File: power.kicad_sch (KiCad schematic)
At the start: 0 parts

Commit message: power sheet
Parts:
- added C1, C10, C15, C16, C21, C22, C4, C9: 1u, symbol Device:C_Small
- added C11, C13, C17, C19, C2, C23, C5, C7: 10u, symbol Device:C_Small
- added C12, C14, C18, C20, C24, C3, C6, C8: 100n, symbol Device:C_Small
- added L1, L2, L3, L4: 4u7, symbol Device:L_Small
- added R1, R7: 40k2, symbol Device:R_Small
- added R10: 249k, symbol Device:R_Small
- added R11: 20k5, symbol Device:R_Small
- added R12: 41k2, symbol Device:R_Small
- added R13, R4, R5, R9: 1k, symbol Device:R_Small
- added R14, R3: 75k, symbol Device:R_Small
- added R15: 11.375k, symbol Device:R_Small
- added R16, R2: 13k, symbol Device:R_Small
- added R6: 120k, symbol Device:R_Small
- added R8: 32k4, symbol Device:R_Small
- added TP1, TP4: 3V3, symbol Connector:TestPoint
- added TP2: 1V8, symbol Connector:TestPoint
- added TP3: 1V2, symbol Connector:TestPoint
- added U1, U2, U3, U4: MP1470, Package_TO_SOT_SMD:TSOT-23-6, symbol Regulator_Switching:MP1470
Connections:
- new net: C22.2, L4.1, U4.2 (SW)
- new net: R14.1, U4.4 (FB)
- new net: C21.1, R13.2, U4.5 (EN)
- new net: C22.1, U4.6 (BST)
- new net: R6.2, R7.2, R8.1
- new net: C1.2, L1.1, U1.2 (SW)
- new net: R6.1, U2.4 (FB)
- new net: R14.2, R15.2, R16.1
- new net: R3.1, U1.4 (FB)
- new net: C4.1, R4.2, U1.5 (EN)
- new net: C1.1, U1.6 (BST)
- new net: C9.1, R5.2, U2.5 (EN)
- new net: C16.2, L3.1, U3.2 (SW)
- new net: C15.1, R9.2, U3.5 (EN)
- new net: R10.2, R11.2, R12.1
- new net: C10.2, L2.1, U2.2 (SW)
- new net: C10.1, U2.6 (BST)
- new net: R1.2, R2.1, R3.2
- new net: R10.1, U3.4 (FB)
- new net: C16.1, U3.6 (BST)
- new net +1V2: C17.1, C18.1, L3.2, R11.1, TP3.1
- new net +1V5: C23.1, C24.1, L4.2, R15.1, TP4.1
- new net +1V8: C11.1, C12.1, L2.2, R7.1, TP2.1
- new net +3V3: C2.1, C3.1, L1.2, R1.1, TP1.1
- new net GND: C11.2, C12.2, C13.2, C14.2, C15.2, C17.2, C18.2, C19.2, C2.2, C20.2, C21.2, C23.2, C24.2, C3.2, C4.2, C5.2, C6.2, C7.2, C8.2, C9.2, R12.2, R16.2, R2.2, R8.2, U1.1 (GND), U2.1 (GND), U3.1 (GND), U4.1 (GND)
- new net VCC: C13.1, C14.1, C19.1, C20.1, C5.1, C6.1, C7.1, C8.1, R13.1, R4.1, R5.1, R9.1, U1.3 (IN), U2.3 (IN), U3.3 (IN), U4.3 (IN)
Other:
- note added: "+1V2 Rail"
- note added: "+1V5 Rail"
- note added: "+1V8 Rail"
- note added: "+3V3 Rail"

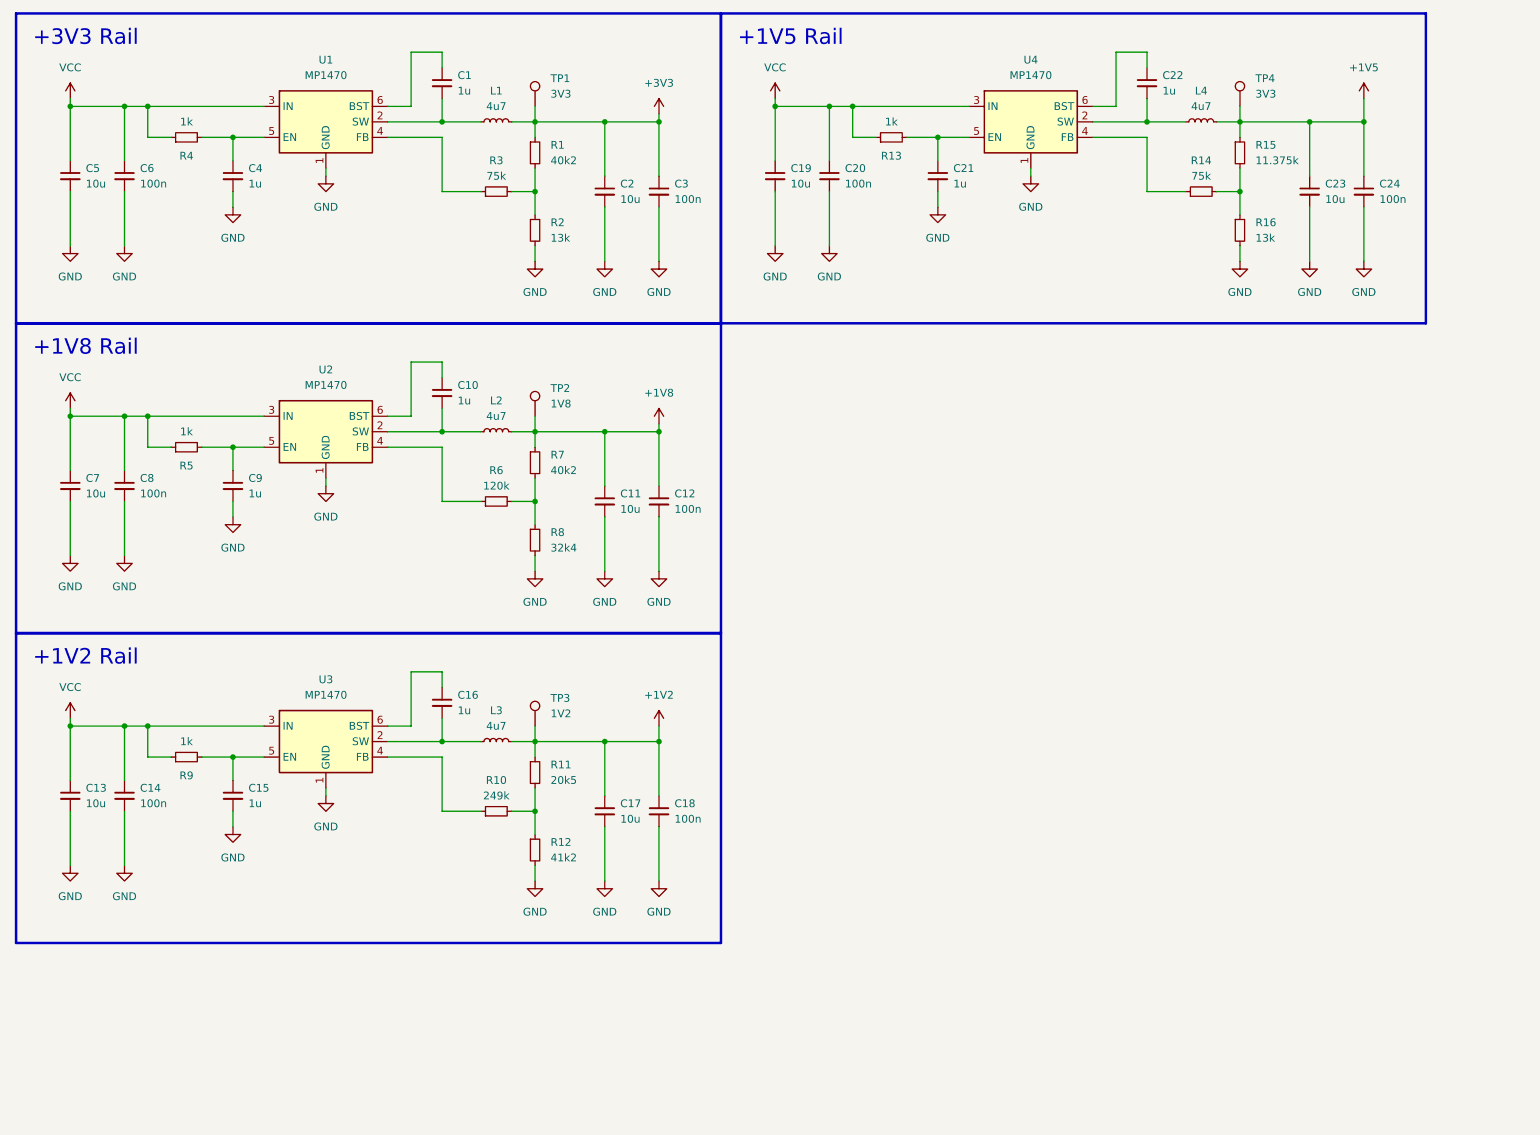
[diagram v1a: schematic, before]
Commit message: more power schematics, adding esd protection and reverse polarity protection and also a fuse.
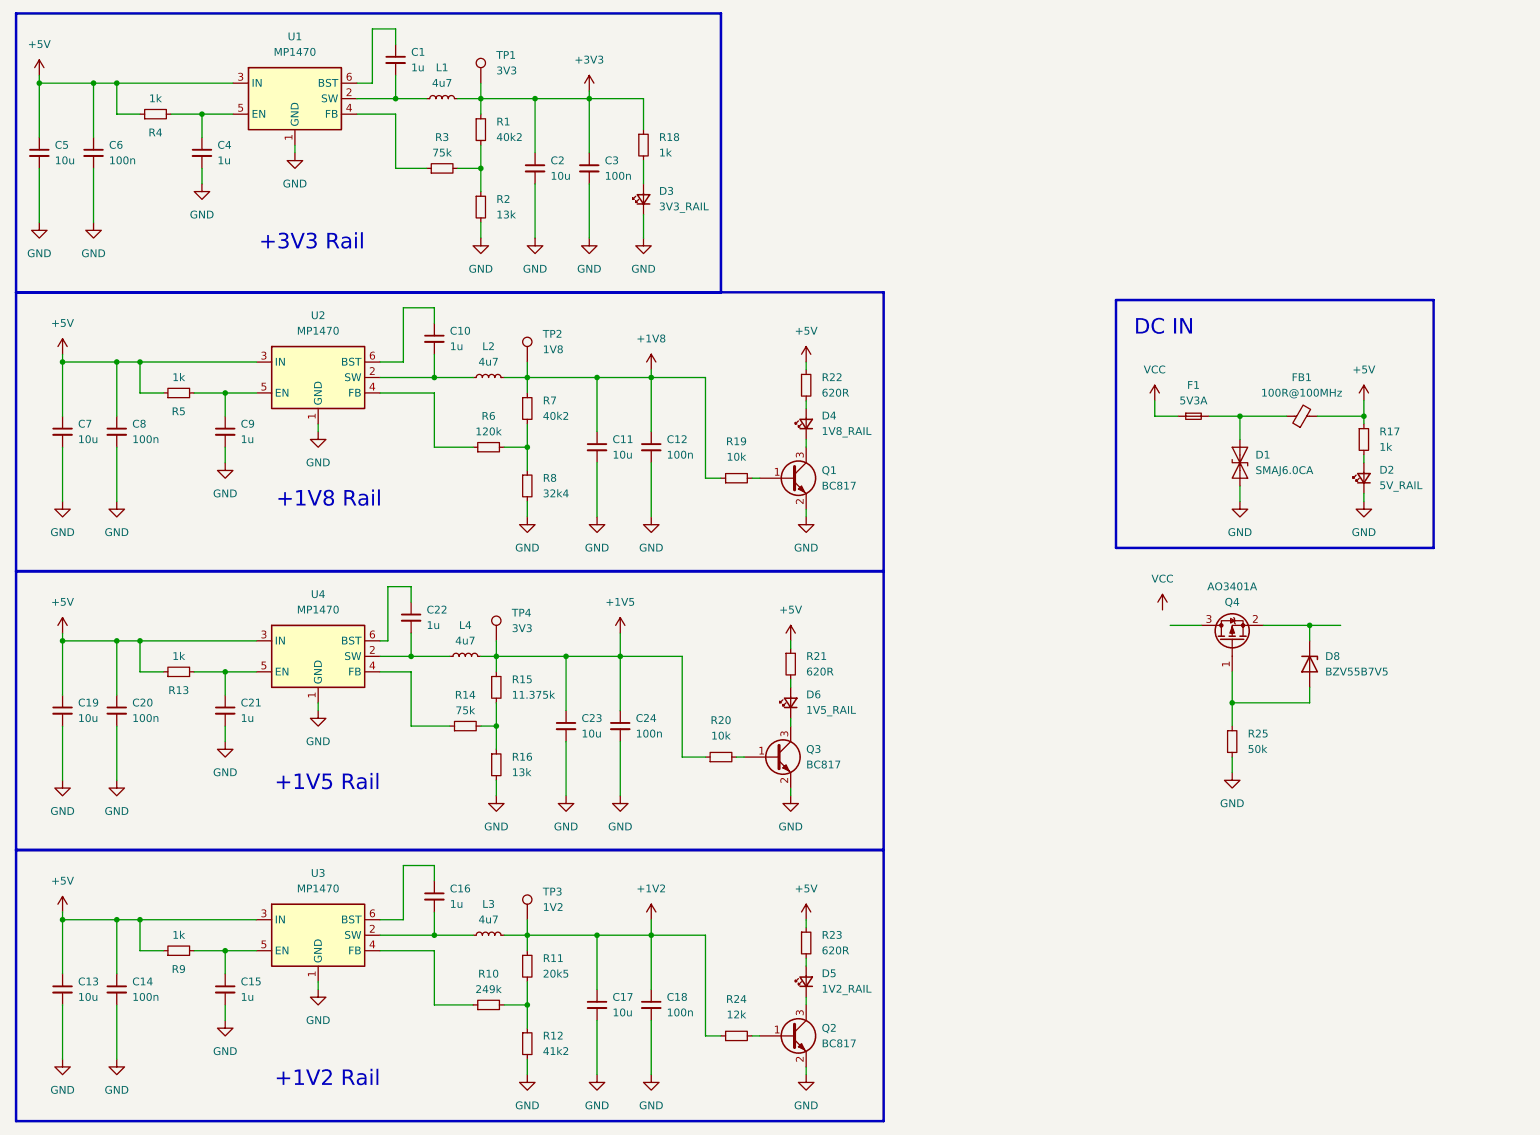
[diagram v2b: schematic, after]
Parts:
- added D1: SMAJ6.0CA, Diode_SMD:D_SMA, symbol Diode:SMAJ6.0CA
- added D2: 5V_RAIL, symbol Device:LED_Small
- added D3: 3V3_RAIL, symbol Device:LED_Small
- added D4: 1V8_RAIL, symbol Device:LED_Small
- added D5: 1V2_RAIL, symbol Device:LED_Small
- added D6: 1V5_RAIL, symbol Device:LED_Small
- added D8: BZV55B7V5, Diode_SMD:D_MiniMELF, symbol Diode:BZV55B7V5
- added F1: 5V3A, symbol Device:Fuse_Small
- added FB1: 100R@100MHz, symbol Device:FerriteBead_Small
- added Q1, Q2, Q3: BC817, Package_TO_SOT_SMD:SOT-23, symbol Transistor_BJT:BC817
- added Q4: AO3401A, Package_TO_SOT_SMD:SOT-23, symbol Transistor_FET:AO3401A
- added R17, R18: 1k, symbol Device:R_Small
- added R19, R20: 10k, symbol Device:R_Small
- added R21, R22, R23: 620R, symbol Device:R_Small
- added R24: 12k, symbol Device:R_Small
- added R25: 50k, symbol Device:R_Small
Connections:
- net +1V2: now also R24.1
- net +1V5: now also R20.1
- net +1V8: now also R19.1
- net +3V3: now also R18.1
- net GND: now also D1.1 (A1), D2.1 (K), D3.1 (K), Q1.2 (E), Q2.2 (E), Q3.2 (E), R25.2
- net VCC: now also F1.1; no longer C13.1, C14.1, C19.1, C20.1, C5.1, C6.1, C7.1, C8.1, R13.1, R4.1, R5.1, R9.1, U1.3 (IN), U2.3 (IN), U3.3 (IN), U4.3 (IN)
- new net: D6.1 (K), Q3.3 (C)
- new net: D6.2 (A), R21.2
- new net: Q1.1 (B), R19.2
- new net: D4.1 (K), Q1.3 (C)
- new net: D1.2 (A2), F1.2, FB1.1
- new net: D4.2 (A), R22.2
- new net: D2.2 (A), R17.2
- new net: D5.2 (A), R23.2
- new net: Q3.1 (B), R20.2
- new net: Q2.1 (B), R24.2
- new net: D8.1 (K), Q4.2 (S)
- new net: D8.2 (A), Q4.1 (G), R25.1
- new net: D5.1 (K), Q2.3 (C)
- new net: D3.2 (A), R18.2
- new net +5V: C13.1, C14.1, C19.1, C20.1, C5.1, C6.1, C7.1, C8.1, FB1.2, R13.1, R17.1, R21.1, R22.1, R23.1, R4.1, R5.1, R9.1, U1.3 (IN), U2.3 (IN), U3.3 (IN), U4.3 (IN)
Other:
- note added: "DC IN"
- moved on the sheet: C1, C10, C11, C12, C13, C14, C15, C16, C17, C18, C19, C2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

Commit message: first prototype. power sheet done
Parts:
- removed D8: BZV55B7V5, Diode_SMD:D_MiniMELF, symbol Diode:BZV55B7V5
- added D7: BZV55B5V6, Diode_SMD:D_MiniMELF, symbol Diode:BZV55B5V6
- R25: value 50k -> 10k
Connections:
- net VCC: now also D1.2 (A2), Q4.3 (D); no longer F1.1
- net at F1.2, FB1.1: no longer D1.2 (A2)
- net at Q4.2 (S): now also F1.1, D7.1 (K)
- net at Q4.1 (G), R25.1: now also D7.2 (A)
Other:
- moved on the sheet: D2, F1, FB1, Q4, R17, R25
